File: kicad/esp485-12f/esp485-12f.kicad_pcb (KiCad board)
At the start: 2 copper layers, 33 x 20.3 mm, 20 parts, among them J1 Conn_01x04, SW1 SW_Push, SW2 SW_Push, U1 MAX3485, U2 ESP-12F, U3 AMS1117-3.3

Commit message: new pcb done
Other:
- rule via_min_size: 0.4 -> 0.8
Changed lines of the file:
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@@
   (general
     (thickness 1.6)
-    (drawings 11)
+    (drawings 12)
     (tracks 181)
     (zones 0)
@@
     (via_size 0.8)
     (via_drill 0.4)
-    (via_min_size 0.4)
+    (via_min_size 0.8)
     (via_min_drill 0.3)
     (uvia_size 0.3)
@@
     (visible_elements FFFFFF7F)
     (pcbplotparams
-      (layerselection 0x010fc_ffffffff)
-      (usegerberextensions false)
+      (layerselection 0x010f0_ffffffff)
+      (usegerberextensions true)
       (usegerberattributes false)
       (usegerberadvancedattributes false)
@@
       (psa4output false)
       (plotreference true)
-      (plotvalue true)
+      (plotvalue false)
       (plotinvisibletext false)
       (padsonsilk false)
-      (subtractmaskfromsilk false)
+      (subtractmaskfromsilk true)
       (outputformat 1)
       (mirror false)
-      (drillshape 1)
+      (drillshape 0)
       (scaleselection 1)
       (outputdirectory ""))
@@
     )
   )
+  (dimension 33.020244 (width 0.3) (layer Cmts.User)
+    (gr_text "33.020 mm" (at 123.190122 133.545) (layer Cmts.User)
+      (effects (font (size 1.5 1.5) (thickness 0.3)))
+    )
+    (feature1 (pts (xy 139.700244 130.048) (xy 139.700244 132.031421)))
+    (feature2 (pts (xy 106.68 130.048) (xy 106.68 132.031421)))
+    (crossbar (pts (xy 106.68 131.445) (xy 139.700244 131.445)))
+    (arrow1a (pts (xy 139.700244 131.445) (xy 138.57374 132.031421)))
+    (arrow1b (pts (xy 139.700244 131.445) (xy 138.57374 130.858579)))
+    (arrow2a (pts (xy 106.68 131.445) (xy 107.806504 132.031421)))
+    (arrow2b (pts (xy 106.68 131.445) (xy 107.806504 130.858579)))
+  )
   (gr_text . (at 129.286 120.65) (layer B.SilkS)
     (effects (font (size 1.5 1.5) (thickness 0.3)) (justify mirror))
@@
     (arrow2b (pts (xy 149.86 107.95) (xy 150.446421 109.076504)))
   )
-  (dimension 40.64 (width 0.3) (layer Cmts.User)
-    (gr_text "40.640 mm" (at 125.73 103.31) (layer Cmts.User)
+  (dimension 39.878 (width 0.3) (layer Cmts.User)
+    (gr_text "39.878 mm" (at 126.111 103.31) (layer Cmts.User)
       (effects (font (size 1.5 1.5) (thickness 0.3)))
     )
-    (feature1 (pts (xy 105.41 106.68) (xy 105.41 104.823579)))
+    (feature1 (pts (xy 106.172 106.68) (xy 106.172 104.823579)))
     (feature2 (pts (xy 146.05 106.68) (xy 146.05 104.823579)))
-    (crossbar (pts (xy 146.05 105.41) (xy 105.41 105.41)))
-    (arrow1a (pts (xy 105.41 105.41) (xy 106.536504 104.823579)))
-    (arrow1b (pts (xy 105.41 105.41) (xy 106.536504 105.996421)))
+    (crossbar (pts (xy 146.05 105.41) (xy 106.172 105.41)))
+    (arrow1a (pts (xy 106.172 105.41) (xy 107.298504 104.823579)))
+    (arrow1b (pts (xy 106.172 105.41) (xy 107.298504 105.996421)))
     (arrow2a (pts (xy 146.05 105.41) (xy 144.923496 104.823579)))
     (arrow2b (pts (xy 146.05 105.41) (xy 144.923496 105.996421)))
@@
   (segment (start 123.539846 117.951846) (end 132.816152 117.951846) (width 0.25) (layer F.Cu) (net 13))
   (segment (start 137.16 113.861996) (end 137.16 111.125) (width 0.25) (layer F.Cu) (net 13))
-  (via (at 133.223 108.712) (size 0.8) (drill 0.4) (layers F.Cu B.Cu) (net 19))
-  (segment (start 133.180666 110.1) (end 133.180666 108.754334) (width 0.25) (layer B.Cu) (net 19))
-  (segment (start 133.180666 108.754334) (end 133.223 108.712) (width 0.25) (layer B.Cu) (net 19))
-  (segment (start 133.223 111.062) (end 133.16 111.125) (width 0.25) (layer F.Cu) (net 19))
-  (segment (start 133.223 108.712) (end 133.223 111.062) (width 0.25) (layer F.Cu) (net 19))
   (via (at 129.159 127.508) (size 0.8) (drill 0.4) (layers F.Cu B.Cu) (net 14))
   (segment (start 129.159 126.12) (end 129.159 127.508) (width 0.25) (layer B.Cu) (net 14))
@@
   (segment (start 127.09541 116.332) (end 126.826 116.332) (width 0.25) (layer B.Cu) (net 18))
   (segment (start 126.826 116.332) (end 126.61 116.116) (width 0.25) (layer B.Cu) (net 18))
+  (via (at 133.223 108.712) (size 0.8) (drill 0.4) (layers F.Cu B.Cu) (net 19))
+  (segment (start 133.180666 110.1) (end 133.180666 108.754334) (width 0.25) (layer B.Cu) (net 19))
+  (segment (start 133.180666 108.754334) (end 133.223 108.712) (width 0.25) (layer B.Cu) (net 19))
+  (segment (start 133.223 111.062) (end 133.16 111.125) (width 0.25) (layer F.Cu) (net 19))
+  (segment (start 133.223 108.712) (end 133.223 111.062) (width 0.25) (layer F.Cu) (net 19))
   (segment (start 133.180666 110.1) (end 135.170332 110.1) (width 0.25) (layer B.Cu) (net 19))
   (zone (net 2) (net_name GND) (layer F.Cu) (hatch edge 0.508)

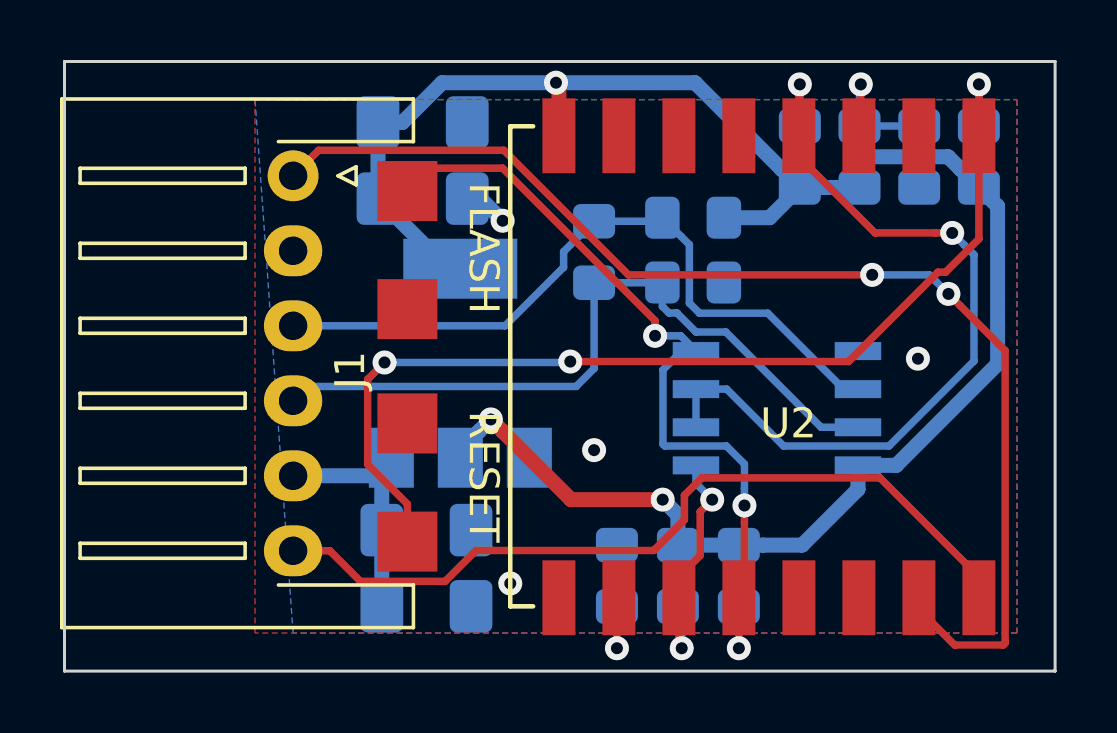
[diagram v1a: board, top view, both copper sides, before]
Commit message: migrated to single wire half duplex method
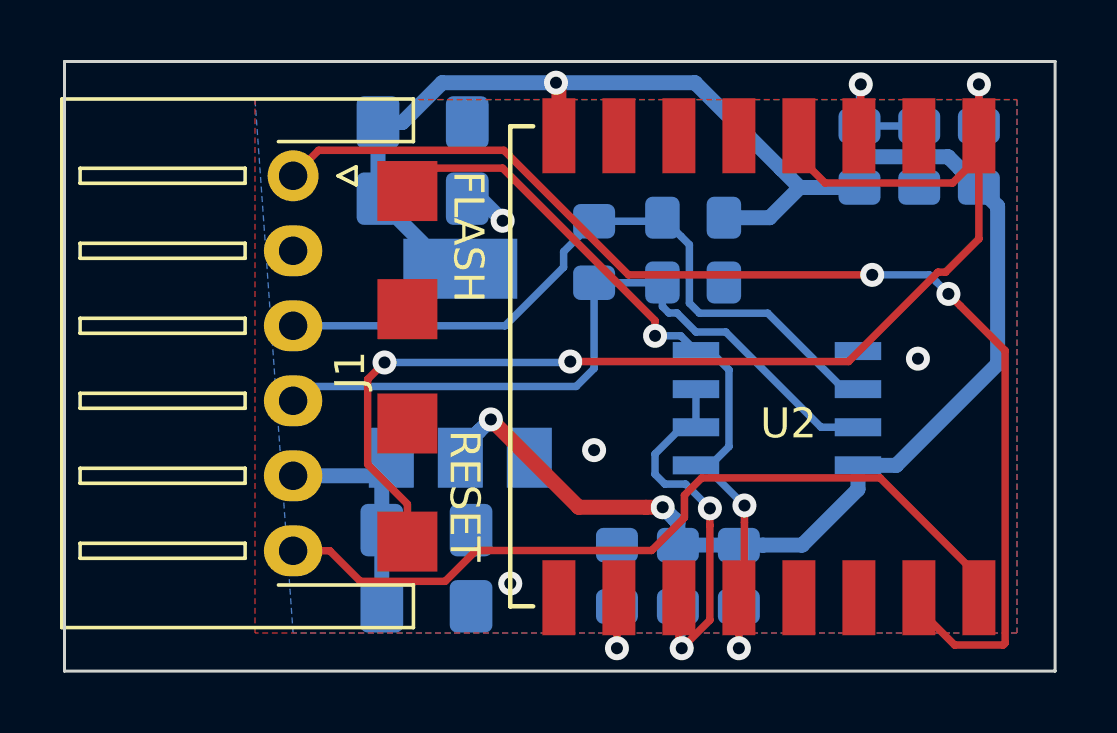
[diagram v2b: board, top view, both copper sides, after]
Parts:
- removed R8: 10K, Resistor_SMD:R_0805_2012Metric_Pad1.15x1.40mm_HandSolder
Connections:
- U1 pad 1: /IO2 -> /IO0
- U1 pad 2: /IO16 -> /IO2
- U1 pad 3: /IO16 -> /IO2
- U2 pad 13: Net-(U2-Pad13) -> (no net)
- U2 pad 14: Net-(U2-Pad14) -> (no net)
- U2 pad 2: Net-(U2-Pad2) -> (no net)
- U2 pad 4: /IO16 -> /RESET
- U2 pad 5: Net-(U2-Pad5) -> (no net)
- U2 pad 6: Net-(U2-Pad6) -> (no net)
- U2 pad 7: Net-(U2-Pad7) -> (no net)
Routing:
- net /IO16: track 27.0 -> 0.00 mm, vias 2 -> 0
- net /RESET: track 34.8 -> 41.5 mm
- net /IO2: track 8.26 -> 14.9 mm

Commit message: remove switches
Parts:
- removed SW1, SW2: SW_Push, tact:tactile_switch_smd_4x3mm_2p
- added C6: C, Capacitor_SMD:C_0805_2012Metric_Pad1.15x1.40mm_HandSolder, B.Cu at (129.5, 111.8)
- added R6: 1K, Resistor_SMD:R_0805_2012Metric_Pad1.15x1.40mm_HandSolder, B.Cu at (131.6, 111.8)
- C3: footprint Capacitor_SMD:C_1206_3216Metric_Pad1.42x1.75mm_HandSolder -> Capacitor_Tantalum_SMD:CP_EIA-7343-15_Kemet-W_Pad2.25x2.55mm_HandSolder
- J1: value Conn_01x04 -> Conn_01x08; footprint Connector_JST:JST_XH_S06B-XH-A-1_1x06_P2.50mm_Horizontal -> Connector_JST:JST_PH_S8B-PH-K_1x08_P2.00mm_Horizontal
- R1, R2, R3, R7, R9: footprint Resistor_SMD:R_0805_2012Metric_Pad1.15x1.40mm_HandSolder -> Resistor_SMD:R_0603_1608Metric_Pad1.05x0.95mm_HandSolder
- moved R5 18.0 mm to (111.0, 122.3), turned to 270 degrees
- moved R4 16.6 mm to (111.0, 113.8), turned to 270 degrees
- moved R3 15.6 mm to (129.5, 124.7)
- moved R1 14.7 mm to (127.5, 124.7)
- moved R10 13.8 mm to (111.0, 118.0)
- moved C5 7.69 mm to (127.5, 111.8), turned to 90 degrees
- moved U2 5.59 mm to (131.6, 111.0)
- moved R7 3.70 mm to (125.5, 124.7), turned to 90 degrees
- moved R2 3.58 mm to (123.6, 124.7), turned to 270 degrees
- moved R9 3.58 mm to (121.5, 124.7)
- moved U1 2.34 mm to (128.7, 118.0)
- moved C3 1.37 mm to (119.8, 113.3)
- moved C1 1.17 mm to (117.6, 123.8)
- moved C2 1.17 mm to (117.6, 126.4)
- moved J1 1.08 mm to (113.5, 111.0)
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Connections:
- J1 pad 1: /RXD -> /IO0
- J1 pad 2: GND -> /RXD
- J1 pad 3: /A -> GND
- J1 pad 4: /B -> /A
- J1 pad 5: VCC -> /B
- J1 pad 6: /TXD -> VCC
- U2 pad 13: (no net) -> Net-(U2-Pad13)
- U2 pad 14: (no net) -> Net-(U2-Pad14)
- U2 pad 2: (no net) -> Net-(U2-Pad2)
- U2 pad 4: /RESET -> Net-(R6-Pad1)
- U2 pad 5: (no net) -> Net-(U2-Pad5)
- U2 pad 6: (no net) -> Net-(U2-Pad6)
- U2 pad 7: (no net) -> Net-(U2-Pad7)
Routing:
- net /RESET: track 41.5 -> 57.2 mm, vias 3 -> 1
- net /IO0: track 26.9 -> 39.2 mm, vias 3 -> 1
- net /RXD: track 41.1 -> 29.0 mm, vias 2 -> 0
- net /EN: track 5.83 -> 14.8 mm
- net +3V3: track 64.9 -> 71.9 mm, vias 3 -> 1
- net Net-(R6-Pad1): track 0.00 -> 6.74 mm, vias 0 -> 1
- net VCC: track 8.61 -> 14.2 mm
- net /TXD: track 26.5 -> 22.0 mm
- net /IO2: track 14.9 -> 12.7 mm, vias 2 -> 1
- net GND: track 1.48 -> 3.54 mm, vias 4 -> 11
- net /IO15: track 3.80 -> 2.22 mm
- net /B: track 24.6 -> 23.1 mm, vias 0 -> 1
- net /A: track 24.1 -> 23.0 mm, vias 0 -> 1
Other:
- board size 33 x 20.3 mm -> 27.3 x 20.3 mm
- board text removed: "FLASH"
- board text removed: "RESET"

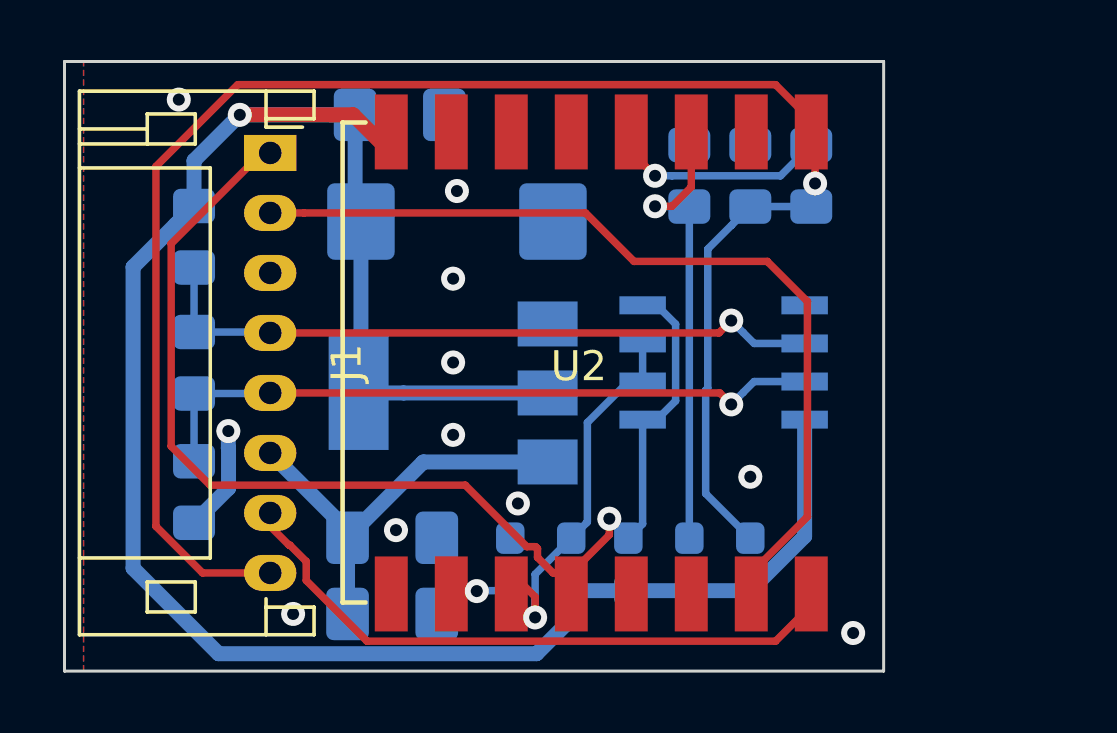
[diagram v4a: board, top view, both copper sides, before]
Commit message: control RS485 DE/!RE separately to save power
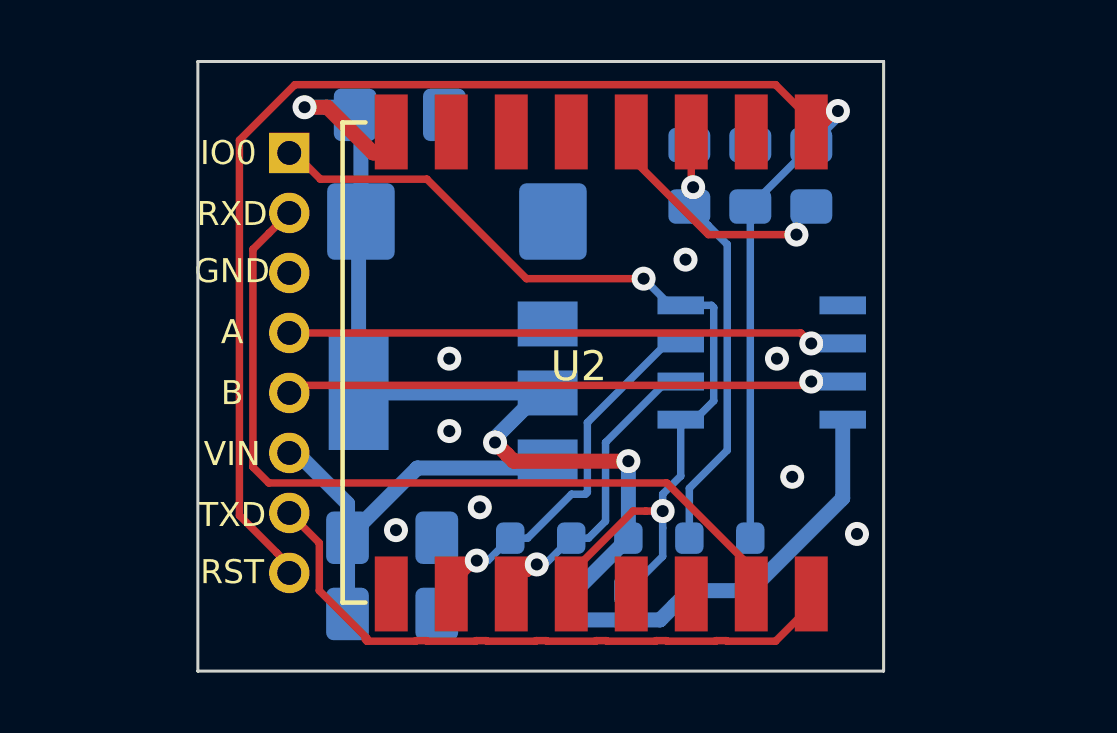
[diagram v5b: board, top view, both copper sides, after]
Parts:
- removed R10: 100, Resistor_SMD:R_0805_2012Metric_Pad1.15x1.40mm_HandSolder
- removed R4, R5: 20K, Resistor_SMD:R_0805_2012Metric_Pad1.15x1.40mm_HandSolder
- J1: footprint Connector_JST:JST_PH_S8B-PH-K_1x08_P2.00mm_Horizontal -> Connector_PinHeader_2.00mm:PinHeader_1x08_P2.00mm_Vertical; moved to B.Cu
- moved U1 1.27 mm to (129.9, 118.0)
- moved J1 0.64 mm to (114.2, 111.0), turned to 180 degrees
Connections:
- net /A renamed A
- net /B renamed B
- net /EN renamed EN
- net /RXD renamed RXD
- net /TXD renamed TXD
- C6 pad 1: /RESET -> RST
- J1 pad 1: /IO0 -> IO0
- J1 pad 8: /RESET -> RST
- R2 pad 1: /IO2 -> IO2
- R3 pad 1: /RESET -> RST
- R6 pad 1: Net-(R6-Pad1) -> RST
- R6 pad 2: /RESET -> IO16
- R7 pad 1: +3V3 -> IO0
- R7 pad 2: /IO0 -> +3V3
- R9 pad 1: /IO15 -> GND
- R9 pad 2: GND -> IO15
- U1 pad 1: /IO0 -> IO0
- U1 pad 2: /IO2 -> IO2
- U1 pad 3: /IO2 -> IO15
- U1 pad 4: /IO0 -> IO0
- U2 pad 1: /RESET -> RST
- U2 pad 10: /IO15 -> IO15
- U2 pad 11: /IO2 -> IO2
- U2 pad 12: /IO0 -> IO0
- U2 pad 13: Net-(U2-Pad13) -> (no net)
- U2 pad 14: Net-(U2-Pad14) -> (no net)
- U2 pad 2: Net-(U2-Pad2) -> (no net)
- U2 pad 4: Net-(R6-Pad1) -> IO16
- U2 pad 5: Net-(U2-Pad5) -> (no net)
- U2 pad 6: Net-(U2-Pad6) -> (no net)
- U2 pad 7: Net-(U2-Pad7) -> (no net)
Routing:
- net /RESET: track 57.2 -> 0.00 mm, vias 1 -> 0
- net RST: track 0.00 -> 53.8 mm, vias 0 -> 1
- net /IO0: track 39.2 -> 0.00 mm, vias 1 -> 0
- net IO0: track 0.00 -> 30.9 mm, vias 0 -> 2
- net +3V3: track 71.9 -> 47.5 mm, vias 1 -> 3
- net /IO2: track 12.7 -> 0.00 mm, vias 1 -> 0
- net IO15: track 0.00 -> 12.2 mm, vias 0 -> 1
- net IO2: track 0.00 -> 9.83 mm, vias 0 -> 1
- net IO16: track 0.00 -> 7.86 mm, vias 0 -> 1
- net Net-(R6-Pad1): track 6.74 -> 0.00 mm, vias 1 -> 0
- net A: track 23.0 -> 18.6 mm
- net B: track 23.1 -> 19.0 mm
- net GND: track 3.54 -> 0.00 mm, vias 11 -> 8
- net /IO15: track 2.22 -> 0.00 mm, vias 1 -> 0
- net RXD: track 29.0 -> 27.2 mm
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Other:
- board size 27.3 x 20.3 mm -> 22.9 x 20.3 mm
- board text added: "A"
- board text added: "B"
- board text added: "GND"
- board text added: "IO0"
- board text added: "RST"
- board text added: "RXD"
- board text added: "TXD"
- board text added: "VIN"
